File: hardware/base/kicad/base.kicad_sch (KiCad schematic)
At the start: 0 parts

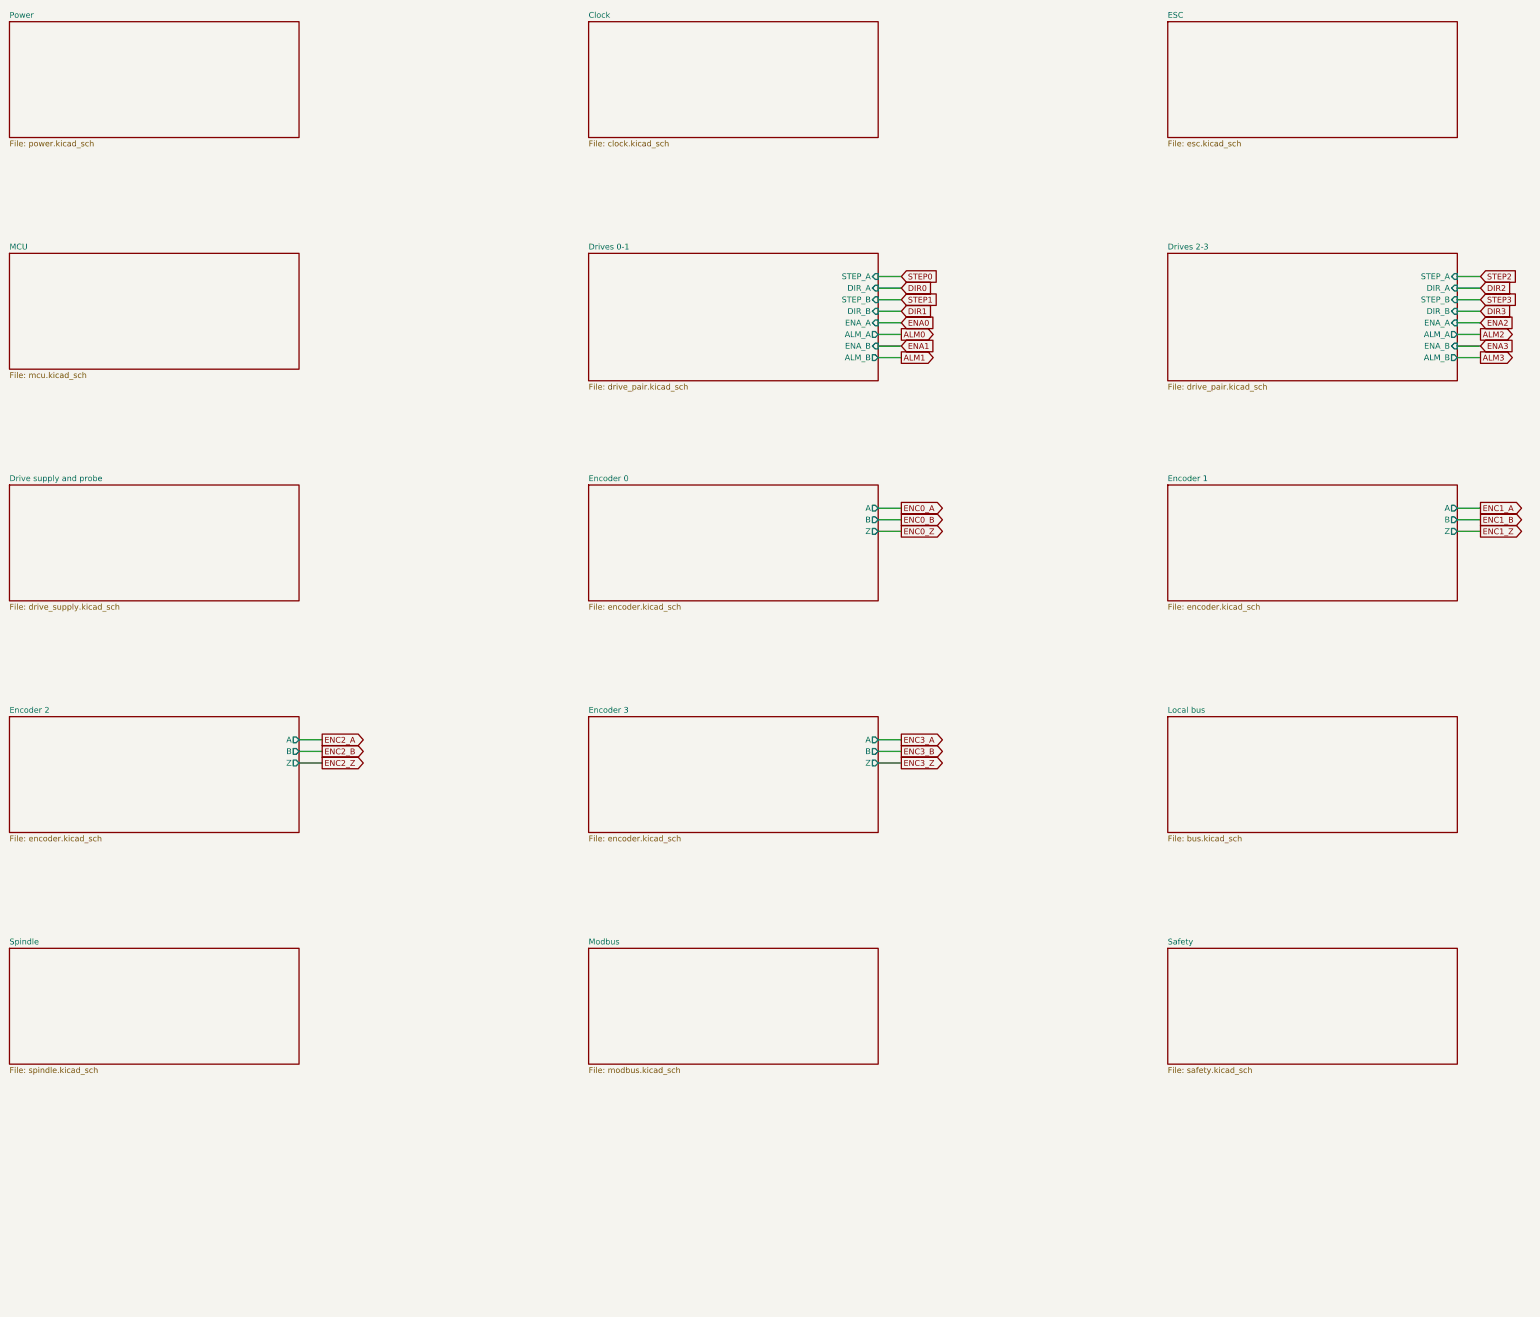
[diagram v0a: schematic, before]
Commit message: One drive sheet per axis with its own dual RS-422 driver; one placement score for every step, block refinement, cost breakdown by block
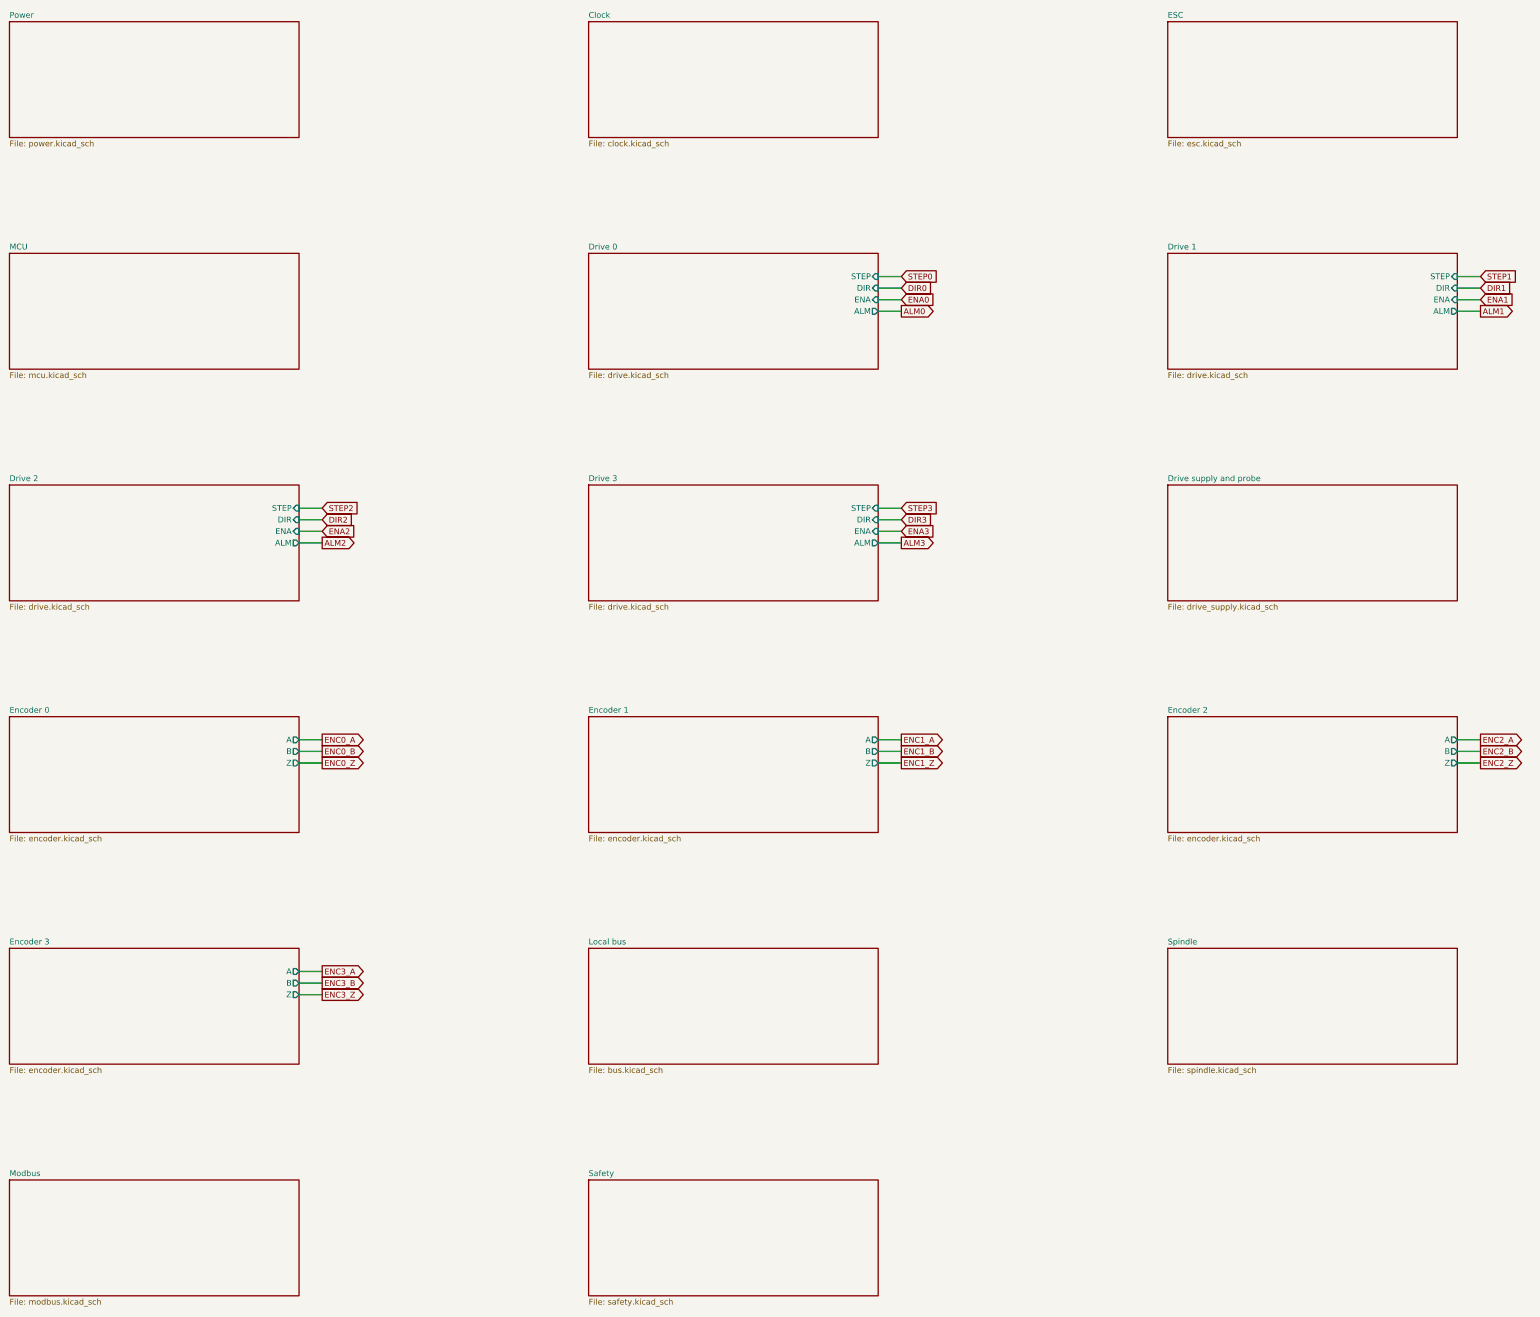
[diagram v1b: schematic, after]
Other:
- removed sheet Drives 0-1
- removed sheet Drives 2-3
- added sheet Drive 0 (drive.kicad_sch)
- added sheet Drive 1 (drive.kicad_sch)
- added sheet Drive 2 (drive.kicad_sch)
- added sheet Drive 3 (drive.kicad_sch)
